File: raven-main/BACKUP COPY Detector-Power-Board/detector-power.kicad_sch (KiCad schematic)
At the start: 43 parts, among them J1 DeployLipo, J2 Conn_01x06, J9 UCLipo, Q1 CSD18543Q3A, Q2 CSD18543Q3A, U2 TPS43060RTE, U7 TPS7A4701xRGW, U8 TPS7A4701xRGW

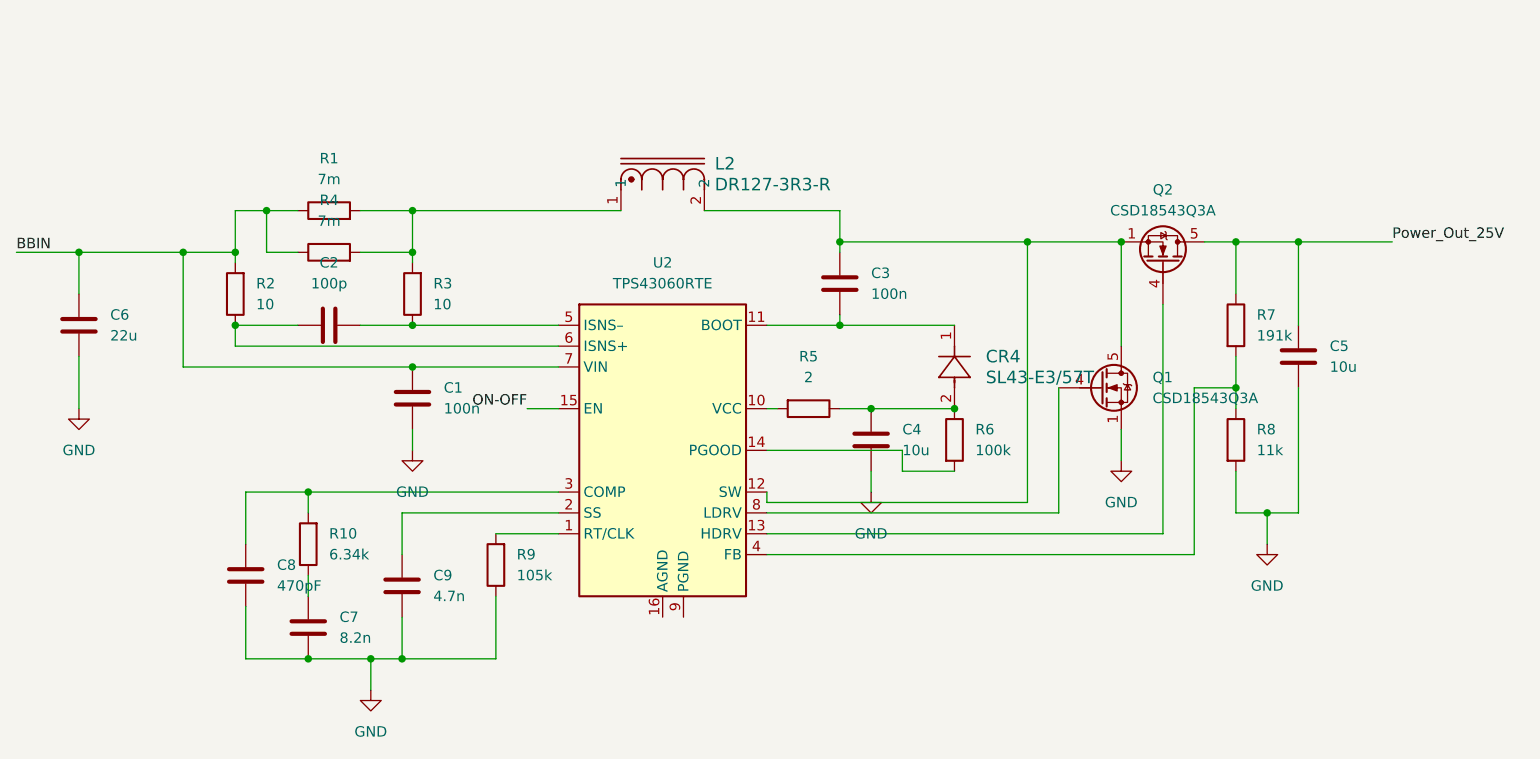
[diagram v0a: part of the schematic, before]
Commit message: Replaced buck boost
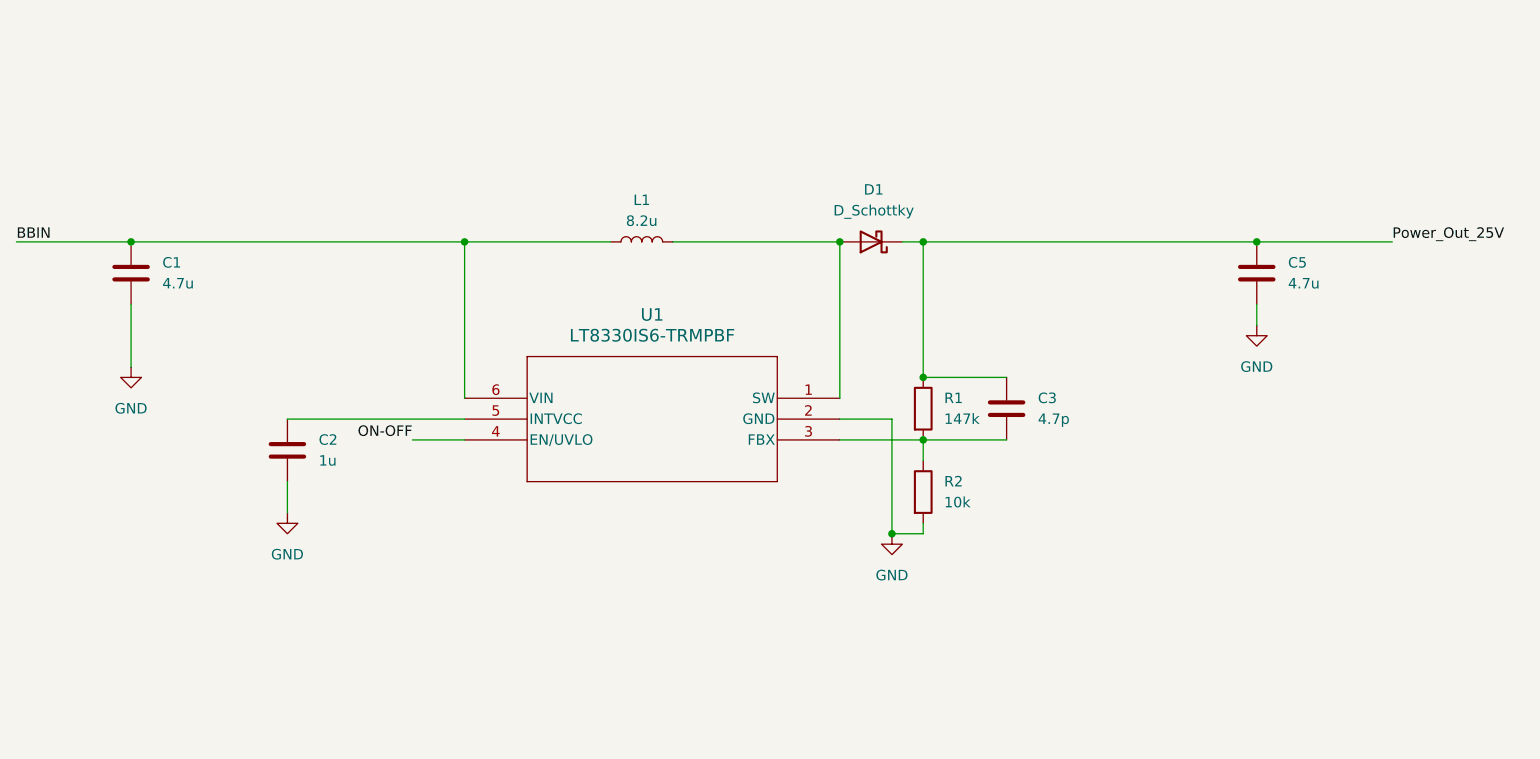
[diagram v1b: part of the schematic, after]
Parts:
- removed C4: 10u, Capacitor_SMD:C_0402_1005Metric, symbol Device:C
- removed C6: 22u, Capacitor_SMD:C_0402_1005Metric, symbol Device:C
- removed C7: 8.2n, Capacitor_SMD:C_0402_1005Metric, symbol Device:C
- removed C8: 470pF, Capacitor_SMD:C_0402_1005Metric, symbol Device:C
- removed C9: 4.7n, Capacitor_SMD:C_0402_1005Metric, symbol Device:C
- removed CR4: SL43-E3/57T, SL43-E3-57T:DIODE_DO214AB, symbol 2026-08-05_22-06-24:SL43-E3_57T
- removed L2: DR127-3R3-R, DR127-3R3-R:DR127, symbol DR127:DR127-3R3-R
- removed Q1, Q2: CSD18543Q3A, Package_SON:VSON-8_3.3x3.3mm_P0.65mm_NexFET, symbol Transistor_FET:CSD18543Q3A
- removed R10: 6.34k, Resistor_SMD:R_0402_1005Metric, symbol Device:R
- removed R3: 10, Resistor_SMD:R_0402_1005Metric, symbol Device:R
- removed R4: 7m, Resistor_SMD:R_0402_1005Metric, symbol Device:R
- removed R5: 2, Resistor_SMD:R_0402_1005Metric, symbol Device:R
- removed R6: 100k, Resistor_SMD:R_0402_1005Metric, symbol Device:R
- removed R7: 191k, Resistor_SMD:R_0402_1005Metric, symbol Device:R
- removed R8: 11k, Resistor_SMD:R_0402_1005Metric, symbol Device:R
- removed R9: 105k, Resistor_SMD:R_0402_1005Metric, symbol Device:R
- removed U2: TPS43060RTE, Package_DFN_QFN:Texas_RTE_WQFN-16-1EP_3x3mm_P0.5mm_EP1.2x0.8mm_ThermalVias, symbol Converter_DCDC:TPS43060RTE
- added D1: D_Schottky, PMEG4010BEA:SOD323F_NEX, symbol Device:D_Schottky
- added L1: 8.2u, CDR7D28MNNP-8R0NC:IND_8R0NC_SUM, symbol Device:L
- added U1: LT8330IS6-TRMPBF, LT8330IS6:IC6_LT8330IS6-TRMPBF_ADI, symbol LT8830:LT8330IS6-TRMPBF
- C1: value 100n -> 4.7u; footprint Capacitor_SMD:C_0402_1005Metric -> Capacitor_SMD:C_0805_2012Metric
- C2: value 100p -> 1u; footprint Capacitor_SMD:C_0402_1005Metric -> Capacitor_SMD:C_0805_2012Metric
- C28, C30, C31, C45, C46, C47: footprint Capacitor_SMD:C_0402_1005Metric -> Capacitor_SMD:C_0805_2012Metric
- C3: value 100n -> 4.7p; footprint Capacitor_SMD:C_0402_1005Metric -> Capacitor_SMD:C_0805_2012Metric
- C5: value 10u -> 4.7u; footprint Capacitor_SMD:C_0402_1005Metric -> Capacitor_SMD:C_0805_2012Metric
- R1: value 7m -> 147k
- R2: value 10 -> 10k
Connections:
- net BBIN: now also L1.1, U1.6 (VIN); no longer R1.1, R2.2
- net GND: now also C2.2, R2.2, U1.2 (GND)
- net ON-OFF: now also U1.4 (EN/UVLO)
- net Power_Out_25V: now also C3.1, R1.1, D1.1 (K)
- net at C3.2: now also R1.2, R2.1, U1.3 (FBX)
- net at C2.1: now also U1.5 (INTVCC); no longer R2.1
- new net: D1.2 (A), L1.2, U1.1 (SW)
